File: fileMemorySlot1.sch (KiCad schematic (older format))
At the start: 4 parts, among them J10 MM1_addressExtension, J8 MM1_receptacle_5530843-2

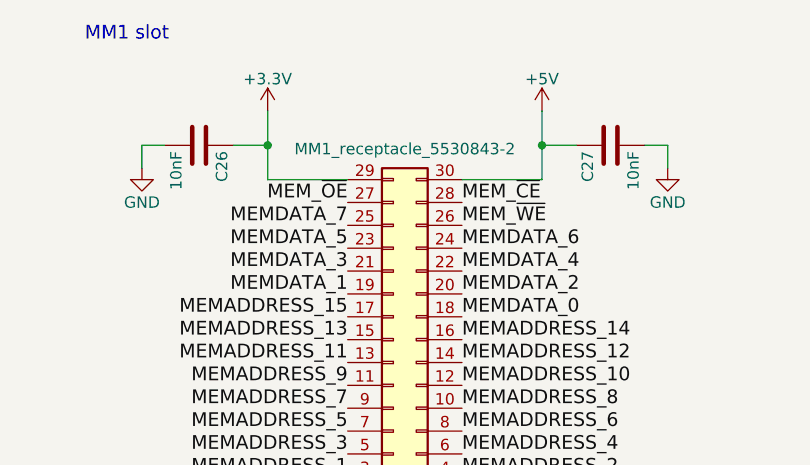
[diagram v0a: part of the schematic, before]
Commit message: V5.1 (#15)
* Remove compatibility for 5.0, 4.x and add 5.1+

* Fix switched pins on SN74LV393A #7

* Removed capacitor on 12V #11

* Add/Modify power decoupling capacitor #10

* Removing ADDSCR_CLK delay #9

* Schematics : set version 5.1, 2021 copyright and publish date

* Put non-electrolytic capacitor #10

* Set every capacitor size to 0805

* Add new footprint for J7 TE_3-641124-6 #6

* Schematic : set pinHeader on J12 #4

* Netlist, apply change to board, clean track, #6 #4 #12 #10

* Set version to 5.1, 2021 copyright and date, replace the missing QRcode

* Back the MM1 connectors #8

* Replace capacitor for U22 U23 U24 #13

* Better decoupling

* Increase version, year to 2021, clear status

* Precise the molex connector for power supply

* First step, import ses

* Clean bottom layer

* #14 Set the BWRITE2 bus instead of BWRITE1 on U12

* netlist, redo autorouting and cleaning

* use shields.io for colored badge

* Update gerbert files

* Changelog, updated BOM

* Small revision on blockDiagram

* Update README.md

* exporting pcb in pdf

* 3D images, diagram.png

* Update schematics pdf

* redo wavedrom_24bitsCounter
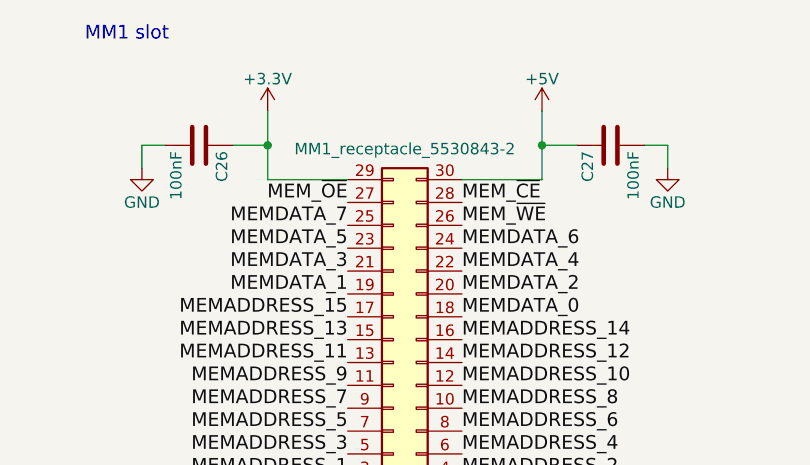
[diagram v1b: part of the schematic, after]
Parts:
- C26, C27: value 10nF -> 100nF
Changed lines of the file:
@@
 Sheet 7 10
 Title "GCM"
-Date "2020-11-23"
-Rev "V5.0"
+Date "2021-02-16"
+Rev "V5.1"
 Comp "Guillaume Guillet"
-Comment1 "Copyright Guillaume Guillet 2020"
+Comment1 "Copyright Guillaume Guillet 2021"
 Comment2 "Licensed under CERN-OHL-W v2 or later"
 Comment3 ""
@@
 AR Path="/5E0692F0/5D5B8D60" Ref="C?"  Part="1"
 F 0 "C26" H 5825 1400 50  0000 L CNN
-F 1 "10nF" H 5825 1200 50  0000 L CNN
+F 1 "100nF" H 5825 1200 50  0000 L CNN
 F 2 "Capacitor_SMD:C_0805_2012Metric" H 5838 1150 50  0001 C CNN
 F 3 "" H 5800 1300 50  0001 C CNN
@@
 AR Path="/5E0692F0/5D5B8D61" Ref="C?"  Part="1"
 F 0 "C27" H 7625 1400 50  0000 L CNN
-F 1 "10nF" H 7625 1200 50  0000 L CNN
+F 1 "100nF" H 7625 1200 50  0000 L CNN
 F 2 "Capacitor_SMD:C_0805_2012Metric" H 7638 1150 50  0001 C CNN
 F 3 "" H 7600 1300 50  0001 C CNN
